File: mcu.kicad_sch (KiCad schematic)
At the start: 55 parts, among them IC5 STM32H723ZGT6, J1 Conn_ST_STDC14, SW1 RESET, Y1 16MHz

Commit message: feat: spare pins
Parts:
- added J5: Conn_01x08, Connector_PinHeader_2.54mm:PinHeader_1x08_P2.54mm_Vertical, symbol Connector_Generic:Conn_01x08
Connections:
- net SPARE_8: now reaches IC5.127 (PG12)
- net SPARE_8: now also J5.4 (Pin_4)
- net SPARE_7: now reaches IC5.128 (PG13)
- net SPARE_7: now also J5.3 (Pin_3)
- net SPARE_6: now reaches IC5.129 (PG14)
- net SPARE_6: now also J5.2 (Pin_2)
- net SPARE_5: now reaches IC5.132 (PG15)
- net SPARE_5: now also J5.1 (Pin_1)
- net SPARE_4: now reaches IC5.134 (PB4)
- net SPARE_4: now also J5.8 (Pin_8)
- net SPARE_3: now reaches IC5.135 (PB5)
- net SPARE_3: now also J5.7 (Pin_7)
- net SPARE_2: now reaches IC5.136 (PB6)
- net SPARE_2: now also J5.6 (Pin_6)
- net SPARE_1: now reaches IC5.137 (PB7)
- net SPARE_1: now also J5.5 (Pin_5)
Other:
- note added: "SPARE PINS"

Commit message: fix: DNPs
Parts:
- J1, J5: now not fitted
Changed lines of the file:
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@@
 		(in_bom yes)
 		(on_board yes)
-		(dnp no)
+		(dnp yes)
 		(property "Reference" "J5"
 			(at 374.396 86.106 0)
@@
 		(in_bom yes)
 		(on_board yes)
-		(dnp no)
+		(dnp yes)
 		(property "Reference" "J1"
 			(at 43.18 228.6 0)

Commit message: feat: production codes
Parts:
- D5, D6: LCSC (none) -> C2286
- D7, SW1: now not fitted; now left out of the parts list
- IC5: LCSC (none) -> C7089881
- R12, R19, R20, R21, R22, R23, R24, R25, R26, R27, R28, R29, R30, R31, R32, R4, R43, R44, R5, R6, R7: value R -> 33R
- Y1: LCSC (none) -> C27869
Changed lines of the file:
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@@
 			)
 		)
-		(property "Value" "R"
+		(property "Value" "33R"
 			(at 231.14 68.58 90)
 			(effects
@@
 		(unit 1)
 		(exclude_from_sim no)
-		(in_bom yes)
+		(in_bom no)
 		(on_board yes)
-		(dnp no)
+		(dnp yes)
 		(property "Reference" "D7"
 			(at 189.23 266.7 90)
@@
 			)
 		)
-		(property "Value" "R"
+		(property "Value" "33R"
 			(at 233.68 209.55 90)
 			(effects
@@
 			)
 		)
-		(property "Value" "R"
+		(property "Value" "33R"
 			(at 238.76 74.93 90)
 			(effects
@@
 			)
 		)
-		(property "Value" "R"
+		(property "Value" "33R"
 			(at 241.3 74.93 90)
 			(effects
@@
 			)
 		)
+		(property "LCSC" "C27869"
+			(at 55.88 198.12 0)
+			(effects
+				(font
+					(size 1.27 1.27)
+				)
+				(hide yes)
+			)
+		)
 		(pin "2"
 		)
@@
 			)
 		)
-		(property "Value" "R"
+		(property "Value" "33R"
 			(at 172.72 73.66 90)
 			(effects
@@
 			)
 		)
-		(property "Value" "R"
+		(property "Value" "33R"
 			(at 135.89 102.87 90)
 			(effects
@@
 			)
 		)
-		(property "Value" "R"
+		(property "Value" "33R"
 			(at 135.89 100.33 90)
 			(effects
@@
 			)
 		)
-		(property "Value" "R"
+		(property "Value" "33R"
 			(at 278.13 171.45 90)
 			(effects
@@
 			)
 		)
-		(property "Value" "R"
+		(property "Value" "33R"
 			(at 280.67 125.73 90)
 			(effects
@@
 			)
 		)
-		(property "Value" "R"
+		(property "Value" "33R"
 			(at 223.52 219.71 90)
 			(effects
@@
 		(unit 1)
 		(exclude_from_sim no)
-		(in_bom yes)
+		(in_bom no)
 		(on_board yes)
-		(dnp no)
+		(dnp yes)
 		(fields_autoplaced yes)
 		(property "Reference" "SW1"
@@
 			)
 		)
-		(property "Value" "R"
+		(property "Value" "33R"
 			(at 232.41 269.24 90)
 			(effects
@@
 			)
 		)
+		(property "LCSC" "C2286"
+			(at 382.27 144.78 90)
+			(effects
+				(font
+					(size 1.27 1.27)
+				)
+				(hide yes)
+			)
+		)
 		(pin "1"
 		)
@@
 			)
 		)
-		(property "Value" "R"
+		(property "Value" "33R"
 			(at 220.98 241.3 90)
 			(effects
@@
 			)
 		)
-		(property "Value" "R"
+		(property "Value" "33R"
 			(at 279.4 153.67 90)
 			(effects
@@
 			)
 		)
-		(property "Value" "R"
+		(property "Value" "33R"
 			(at 278.13 168.91 90)
 			(effects
@@
 			)
 		)
-		(property "Value" "R"
+		(property "Value" "33R"
 			(at 238.76 226.06 90)
 			(effects
@@
 			)
 		)
-		(property "Value" "R"
+		(property "Value" "33R"
 			(at 279.4 156.21 90)
 			(effects
@@
 			)
 		)
-		(property "Value" "R"
+		(property "Value" "33R"
 			(at 233.68 68.58 90)
 			(effects
@@
 			)
 		)
-		(property "Value" "R"
+		(property "Value" "33R"
 			(at 218.694 241.554 90)
 			(effects
@@
 			)
 		)
+		(property "LCSC" "C7089881"
+			(at 157.48 97.79 0)
+			(effects
+				(font
+					(size 1.27 1.27)
+				)
+				(hide yes)
+			)
+		)
 		(pin "62"
 		)
@@
 			)
 		)
+		(property "LCSC" "C2286"
+			(at 397.51 144.78 90)
+			(effects
+				(font
+					(size 1.27 1.27)
+				)
+				(hide yes)
+			)
+		)
 		(pin "1"
 		)
@@
 			)
 		)
-		(property "Value" "R"
+		(property "Value" "33R"
 			(at 241.3 226.06 90)
 			(effects
@@
 			)
 		)
-		(property "Value" "R"
+		(property "Value" "33R"
 			(at 280.67 128.27 90)
 			(effects
@@
 			)
 		)
-		(property "Value" "R"
+		(property "Value" "33R"
 			(at 170.18 73.66 90)
 			(effects

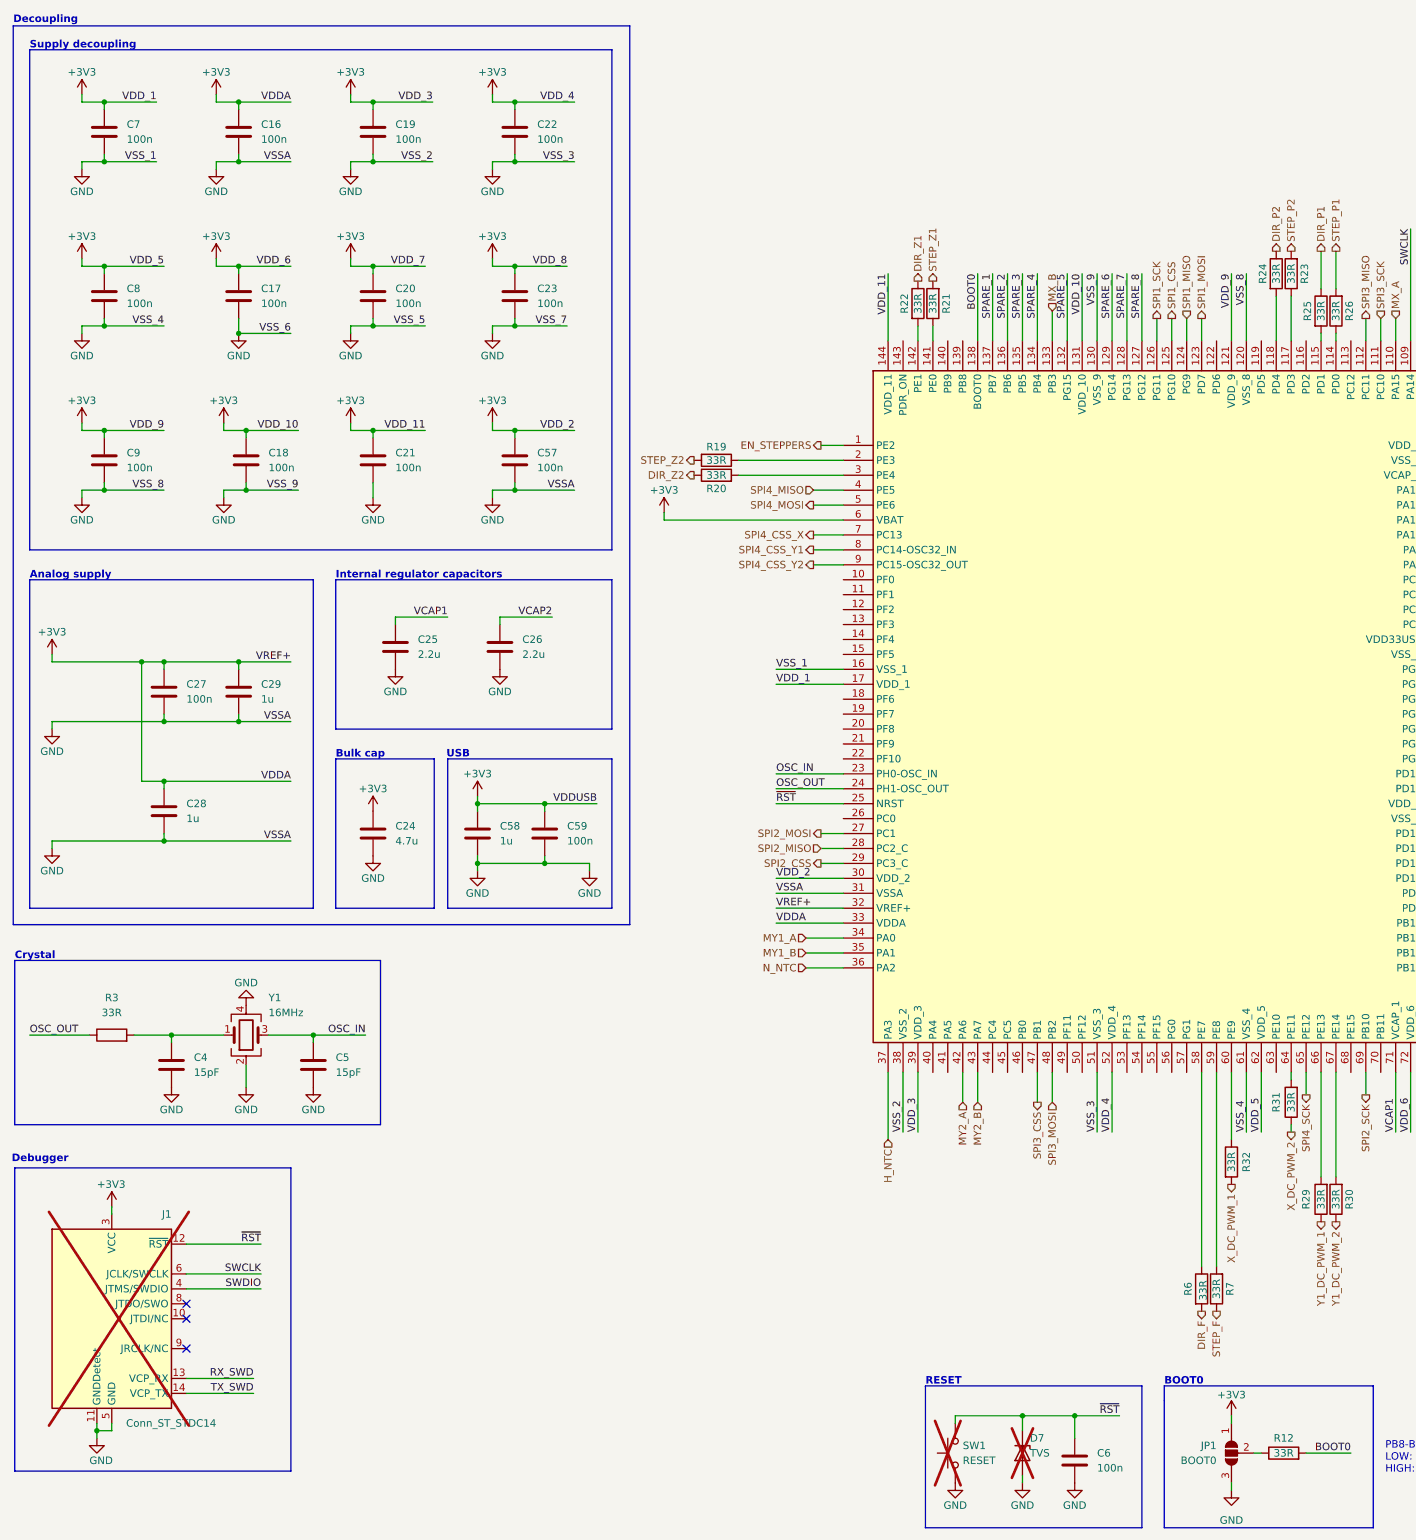
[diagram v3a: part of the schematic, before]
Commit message: fix: remove bl decoupling caps from prod
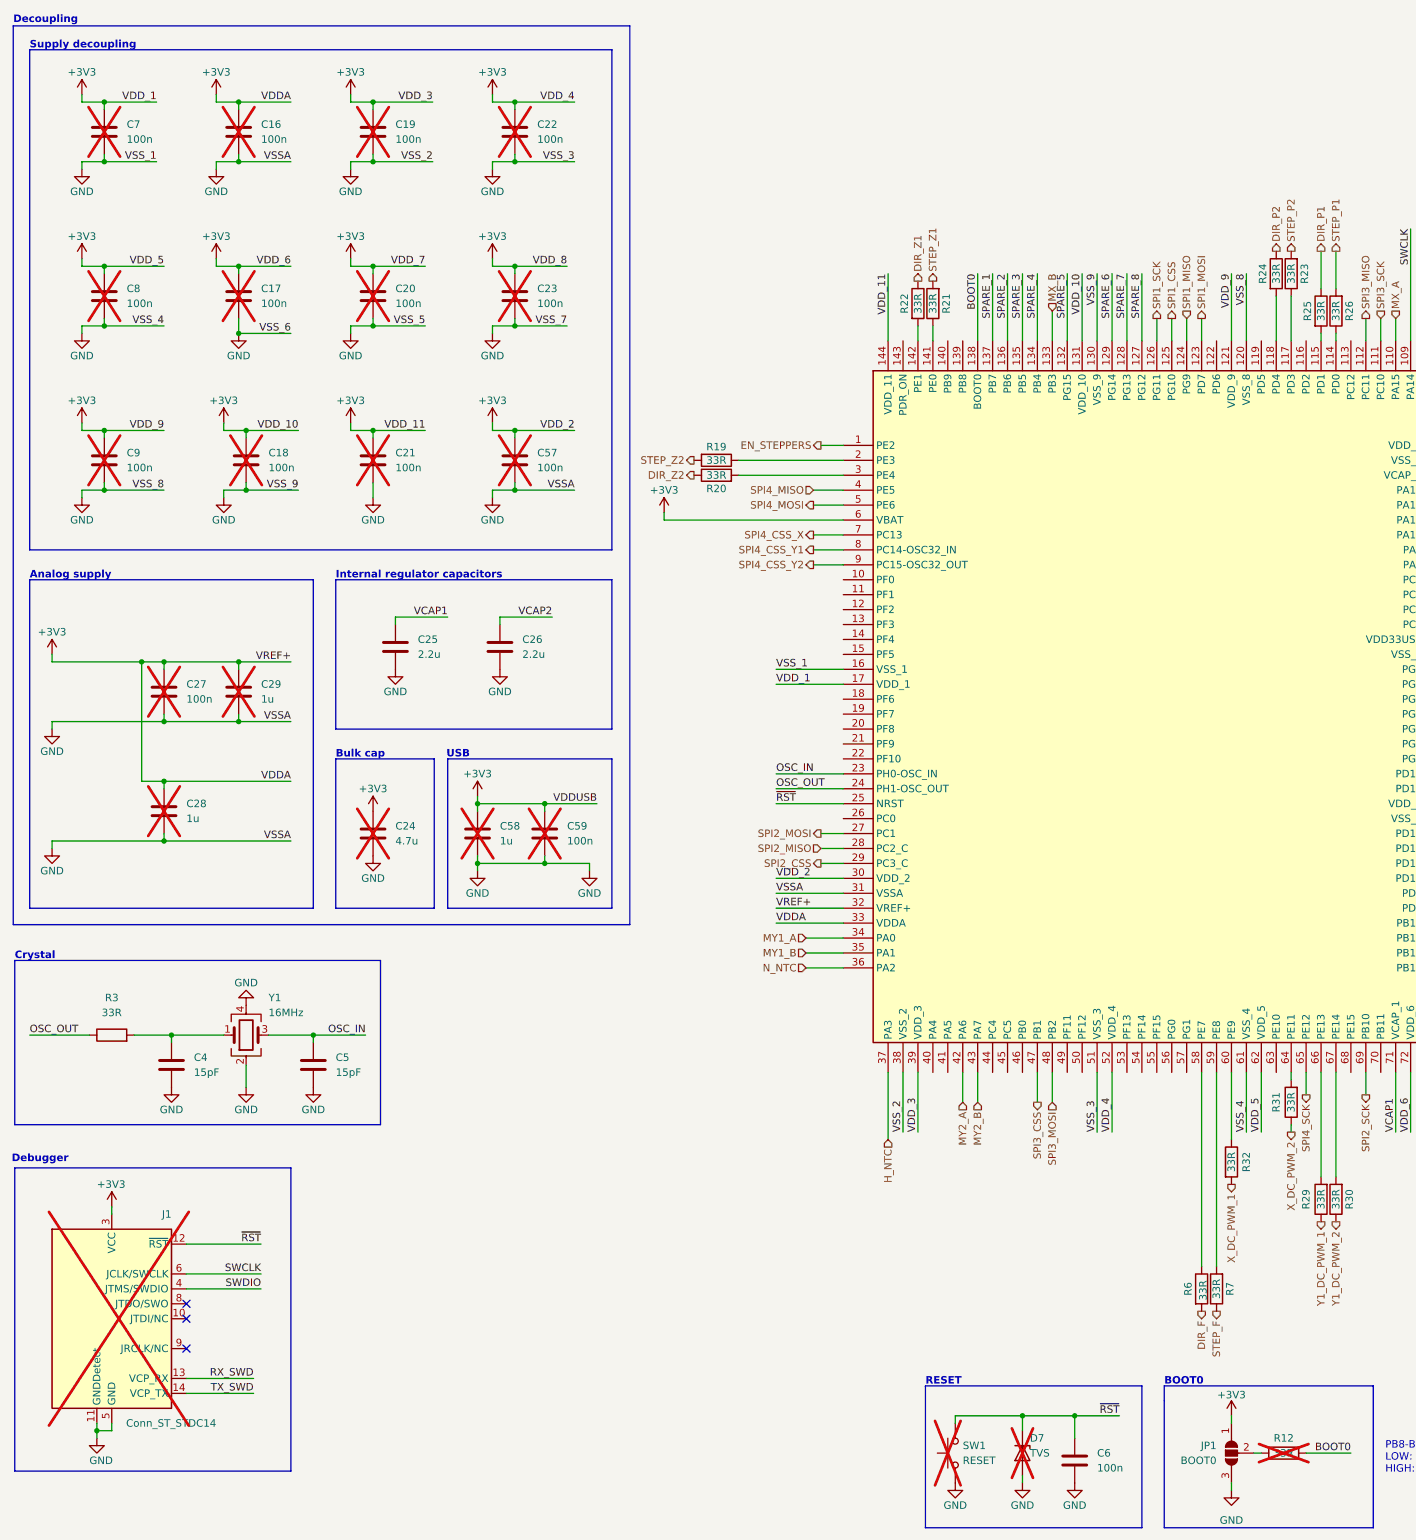
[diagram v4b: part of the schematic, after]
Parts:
- C16, C17, C18, C19, C20, C21, C22, C23, C24, C27, C28, C29, C57, C58, C59, C7, C8, C9, R12: now not fitted; now left out of the parts list
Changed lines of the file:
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@@
 		(unit 1)
 		(exclude_from_sim no)
-		(in_bom yes)
+		(in_bom no)
 		(on_board yes)
-		(dnp no)
+		(dnp yes)
 		(fields_autoplaced yes)
 		(property "Reference" "C7"
@@
 		(unit 1)
 		(exclude_from_sim no)
-		(in_bom yes)
+		(in_bom no)
 		(on_board yes)
-		(dnp no)
+		(dnp yes)
 		(fields_autoplaced yes)
 		(property "Reference" "C21"
@@
 		(unit 1)
 		(exclude_from_sim no)
-		(in_bom yes)
+		(in_bom no)
 		(on_board yes)
-		(dnp no)
+		(dnp yes)
 		(fields_autoplaced yes)
 		(property "Reference" "C22"
@@
 		(unit 1)
 		(exclude_from_sim no)
-		(in_bom yes)
+		(in_bom no)
 		(on_board yes)
-		(dnp no)
+		(dnp yes)
 		(fields_autoplaced yes)
 		(property "Reference" "C23"
@@
 		(unit 1)
 		(exclude_from_sim no)
-		(in_bom yes)
+		(in_bom no)
 		(on_board yes)
-		(dnp no)
+		(dnp yes)
 		(fields_autoplaced yes)
 		(property "Reference" "C24"
@@
 		(unit 1)
 		(exclude_from_sim no)
-		(in_bom yes)
+		(in_bom no)
 		(on_board yes)
-		(dnp no)
+		(dnp yes)
 		(fields_autoplaced yes)
 		(property "Reference" "C9"
@@
 		(unit 1)
 		(exclude_from_sim no)
-		(in_bom yes)
+		(in_bom no)
 		(on_board yes)
-		(dnp no)
+		(dnp yes)
 		(fields_autoplaced yes)
 		(property "Reference" "C20"
@@
 		(unit 1)
 		(exclude_from_sim no)
-		(in_bom yes)
+		(in_bom no)
 		(on_board yes)
-		(dnp no)
+		(dnp yes)
 		(fields_autoplaced yes)
 		(property "Reference" "C27"
@@
 		(unit 1)
 		(exclude_from_sim no)
-		(in_bom yes)
+		(in_bom no)
 		(on_board yes)
-		(dnp no)
+		(dnp yes)
 		(fields_autoplaced yes)
 		(property "Reference" "C59"
@@
 		(unit 1)
 		(exclude_from_sim no)
-		(in_bom yes)
+		(in_bom no)
 		(on_board yes)
-		(dnp no)
+		(dnp yes)
 		(fields_autoplaced yes)
 		(property "Reference" "C57"
@@
 		(unit 1)
 		(exclude_from_sim no)
-		(in_bom yes)
+		(in_bom no)
 		(on_board yes)
-		(dnp no)
+		(dnp yes)
 		(fields_autoplaced yes)
 		(property "Reference" "C28"
@@
 		(unit 1)
 		(exclude_from_sim no)
-		(in_bom yes)
+		(in_bom no)
 		(on_board yes)
-		(dnp no)
+		(dnp yes)
 		(fields_autoplaced yes)
 		(property "Reference" "C18"
@@
 		(unit 1)
 		(exclude_from_sim no)
-		(in_bom yes)
+		(in_bom no)
 		(on_board yes)
-		(dnp no)
+		(dnp yes)
 		(fields_autoplaced yes)
 		(property "Reference" "C29"
@@
 		(unit 1)
 		(exclude_from_sim no)
-		(in_bom yes)
+		(in_bom no)
 		(on_board yes)
-		(dnp no)
+		(dnp yes)
 		(fields_autoplaced yes)
 		(property "Reference" "C8"
@@
 		(unit 1)
 		(exclude_from_sim no)
-		(in_bom yes)
+		(in_bom no)
 		(on_board yes)
-		(dnp no)
+		(dnp yes)
 		(property "Reference" "R12"
 			(at 232.41 266.7 90)
@@
 		(unit 1)
 		(exclude_from_sim no)
-		(in_bom yes)
+		(in_bom no)
 		(on_board yes)
-		(dnp no)
+		(dnp yes)
 		(fields_autoplaced yes)
 		(property "Reference" "C58"
@@
 		(unit 1)
 		(exclude_from_sim no)
-		(in_bom yes)
+		(in_bom no)
 		(on_board yes)
-		(dnp no)
+		(dnp yes)
 		(fields_autoplaced yes)
 		(property "Reference" "C19"
@@
 		(unit 1)
 		(exclude_from_sim no)
-		(in_bom yes)
+		(in_bom no)
 		(on_board yes)
-		(dnp no)
+		(dnp yes)
 		(fields_autoplaced yes)
 		(property "Reference" "C17"
@@
 		(unit 1)
 		(exclude_from_sim no)
-		(in_bom yes)
+		(in_bom no)
 		(on_board yes)
-		(dnp no)
+		(dnp yes)
 		(fields_autoplaced yes)
 		(property "Reference" "C16"

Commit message: fix: root sheet LCSC codes
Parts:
- R10, R11: LCSC (none) -> C177343
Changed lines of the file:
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@@
+			)
+		)
+		(property "LCSC" "C177343"
+			(at 382.27 137.16 0)
+			(effects
+				(font
+					(size 1.27 1.27)
+				)
+				(hide yes)
 			)
 		)
@@
 			(at 397.51 137.16 0)
 			(effects
+				(font
+					(size 1.27 1.27)
+				)
+				(hide yes)
+			)
+		)
+		(property "LCSC" "C177343"
+			(at 397.51 137.16 0)
+			(effects

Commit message: feat: LCSC codes for all components to be soldered
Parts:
- C25, C26: LCSC (none) -> C377773
- C4, C5: LCSC (none) -> C1644
- C6: LCSC (none) -> C14663
- R10, R11: LCSC C177343 -> C21190
- R19, R20, R21, R22, R23, R24, R25, R26, R27, R28, R29, R3, R30, R31, R32, R4, R43, R44, R5, R6, R7: LCSC (none) -> C23140
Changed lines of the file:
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@@
 			)
 		)
+		(property "LCSC" "C23140"
+			(at 231.14 68.58 90)
+			(effects
+				(font
+					(size 1.27 1.27)
+				)
+				(hide yes)
+			)
+		)
 		(pin "1"
 		)
@@
 			)
 		)
+		(property "LCSC" "C23140"
+			(at 233.68 209.55 90)
+			(effects
+				(font
+					(size 1.27 1.27)
+				)
+				(hide yes)
+			)
+		)
 		(pin "1"
 		)
@@
 			)
 		)
+		(property "LCSC" "C23140"
+			(at 238.76 74.93 90)
+			(effects
+				(font
+					(size 1.27 1.27)
+				)
+				(hide yes)
+			)
+		)
 		(pin "1"
 		)
@@
 			)
 		)
+		(property "LCSC" "C23140"
+			(at 241.3 74.93 90)
+			(effects
+				(font
+					(size 1.27 1.27)
+				)
+				(hide yes)
+			)
+		)
 		(pin "1"
 		)
@@
 			)
 		)
+		(property "LCSC" "C377773"
+			(at 81.28 132.08 0)
+			(effects
+				(font
+					(size 1.27 1.27)
+				)
+				(hide yes)
+			)
+		)
 		(pin "2"
 		)
@@
 			)
 		)
+		(property "LCSC" "C23140"
+			(at 33.02 198.12 90)
+			(effects
+				(font
+					(size 1.27 1.27)
+				)
+				(hide yes)
+			)
+		)
 		(pin "2"
 		)
@@
 			)
 		)
+		(property "LCSC" "C23140"
+			(at 172.72 73.66 90)
+			(effects
+				(font
+					(size 1.27 1.27)
+				)
+				(hide yes)
+			)
+		)
 		(pin "1"
 		)
@@
 			)
 		)
+		(property "LCSC" "C23140"
+			(at 135.89 102.87 90)
+			(effects
+				(font
+					(size 1.27 1.27)
+				)
+				(hide yes)
+			)
+		)
 		(pin "1"
 		)
@@
 			)
 		)
+		(property "LCSC" "C23140"
+			(at 135.89 100.33 90)
+			(effects
+				(font
+					(size 1.27 1.27)
+				)
+				(hide yes)
+			)
+		)
 		(pin "1"
 		)
@@
 			)
 		)
+		(property "LCSC" "C23140"
+			(at 278.13 171.45 90)
+			(effects
+				(font
+					(size 1.27 1.27)
+				)
+				(hide yes)
+			)
+		)
 		(pin "1"
 		)
@@
 			)
 		)
+		(property "LCSC" "C1644"
+			(at 43.18 203.2 0)
+			(effects
+				(font
+					(size 1.27 1.27)
+				)
+				(hide yes)
+			)
+		)
 		(pin "1"
 		)
@@
 			)
 		)
+		(property "LCSC" "C23140"
+			(at 280.67 125.73 90)
+			(effects
+				(font
+					(size 1.27 1.27)
+				)
+				(hide yes)
+			)
+		)
 		(pin "1"
 		)
@@
 			)
 		)
+		(property "LCSC" "C23140"
+			(at 223.52 219.71 90)
+			(effects
+				(font
+					(size 1.27 1.27)
+				)
+				(hide yes)
+			)
+		)
 		(pin "1"
 		)
@@
 			)
 		)
-		(property "LCSC" "C177343"
+		(property "LCSC" "C21190"
 			(at 382.27 137.16 0)
 			(effects
@@
 			)
 		)
+		(property "LCSC" "C14663"
+			(at 196.85 270.51 0)
+			(effects
+				(font
+					(size 1.27 1.27)
+				)
+				(hide yes)
+			)
+		)
 		(pin "1"
 		)
@@
 			)
 		)
+		(property "LCSC" "C23140"
+			(at 220.98 241.3 90)
+			(effects
+				(font
+					(size 1.27 1.27)
+				)
+				(hide yes)
+			)
+		)
 		(pin "1"
 		)
@@
 			)
 		)
+		(property "LCSC" "C377773"
+			(at 99.06 132.08 0)
+			(effects
+				(font
+					(size 1.27 1.27)
+				)
+				(hide yes)
+			)
+		)
 		(pin "2"
 		)
@@
 			)
 		)
+		(property "LCSC" "C23140"
+			(at 279.4 153.67 90)
+			(effects
+				(font
+					(size 1.27 1.27)
+				)
+				(hide yes)
+			)
+		)
 		(pin "1"
 		)
@@
 			)
 		)
+		(property "LCSC" "C23140"
+			(at 278.13 168.91 90)
+			(effects
+				(font
+					(size 1.27 1.27)
+				)
+				(hide yes)
+			)
+		)
 		(pin "1"
 		)
@@
 			)
 		)
-		(property "LCSC" "C177343"
+		(property "LCSC" "C21190"
 			(at 397.51 137.16 0)
 			(effects
@@
 			)
 		)
+		(property "LCSC" "C23140"
+			(at 238.76 226.06 90)
+			(effects
+				(font
+					(size 1.27 1.27)
+				)
+				(hide yes)
+			)
+		)
 		(pin "1"
 		)
@@
 			)
 		)
+		(property "LCSC" "C23140"
+			(at 279.4 156.21 90)
+			(effects
+				(font
+					(size 1.27 1.27)
+				)
+				(hide yes)
+			)
+		)
 		(pin "1"
 		)
@@
 			)
 		)
+		(property "LCSC" "C23140"
+			(at 233.68 68.58 90)
+			(effects
+				(font
+					(size 1.27 1.27)
+				)
+				(hide yes)
+			)
+		)
 		(pin "1"
 		)
@@
 			)
 		)
+		(property "LCSC" "C1644"
+			(at 67.31 203.2 0)
+			(effects
+				(font
+					(size 1.27 1.27)
+				)
+				(hide yes)
+			)
+		)
 		(pin "1"
 		)
@@
 			)
 		)
+		(property "LCSC" "C23140"
+			(at 218.44 241.3 90)
+			(effects
+				(font
+					(size 1.27 1.27)
+				)
+				(hide yes)
+			)
+		)
 		(pin "1"
 		)
@@
 			)
 		)
+		(property "LCSC" "C23140"
+			(at 241.3 226.06 90)
+			(effects
+				(font
+					(size 1.27 1.27)
+				)
+				(hide yes)
+			)
+		)
 		(pin "1"
 		)
@@
 			)
 		)
+		(property "LCSC" "C23140"
+			(at 280.67 128.27 90)
+			(effects
+				(font
+					(size 1.27 1.27)
+				)
+				(hide yes)
+			)
+		)
 		(pin "1"
 		)
@@
 			(effects
 				(font
+					(size 1.27 1.27)
+				)
+				(hide yes)
+			)
+		)
+		(property "LCSC" "C23140"
+			(at 170.18 73.66 90)
+			(effects
+				(font

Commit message: fix: prod notes
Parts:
- IC5: JLCPCB Rotation Offset (none) -> 270
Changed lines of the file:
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@@
+			)
+		)
+		(property "JLCPCB Rotation Offset" "270"
+			(at 157.48 97.79 0)
+			(effects
+				(font
+					(size 1.27 1.27)
+				)
+				(hide yes)
 			)
 		)
